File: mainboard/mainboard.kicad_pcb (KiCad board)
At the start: 2 copper layers, 53 x 53 mm, 95 parts, among them J1 USB_B_Micro, J2 Conn_01x19_MountingPin, J3 Conn_01x19_MountingPin, Q1 DMG2301L, Q2 MMBT3904, Q3 MMBT3904, SW1 SW_Push, SW2 SW_Push, U1 ESP32-WROOM-32, U2 tps63070, U3 tps63070, U4 tps63070, U5 CP2102N-A01-GQFN24, U6 BME680, U7 BH1750FVI, U8 LIS3MDL, U9 ADXL343

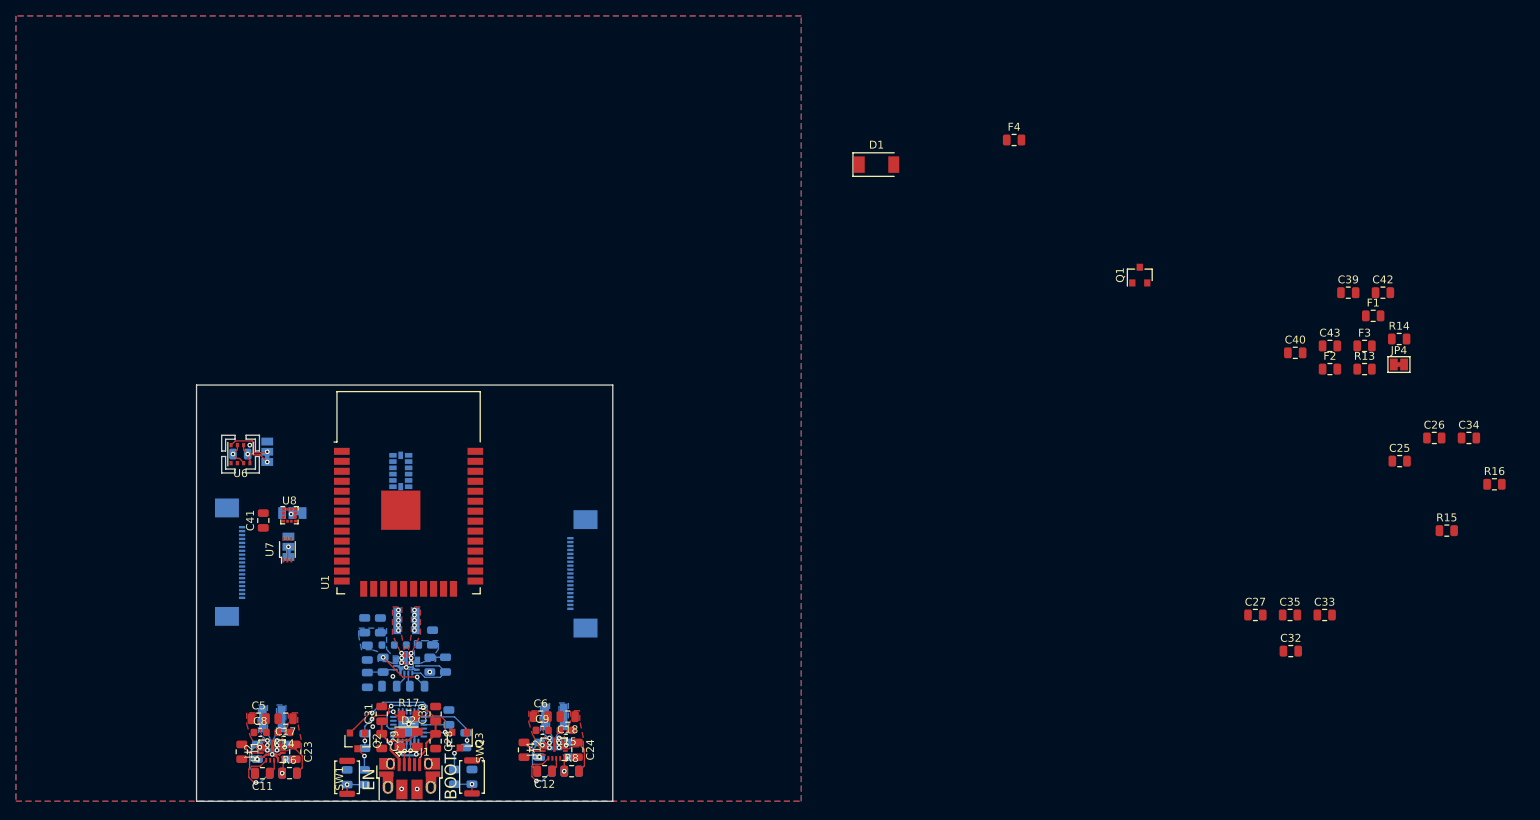
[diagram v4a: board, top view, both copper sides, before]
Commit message: Move components to sane-ish positions
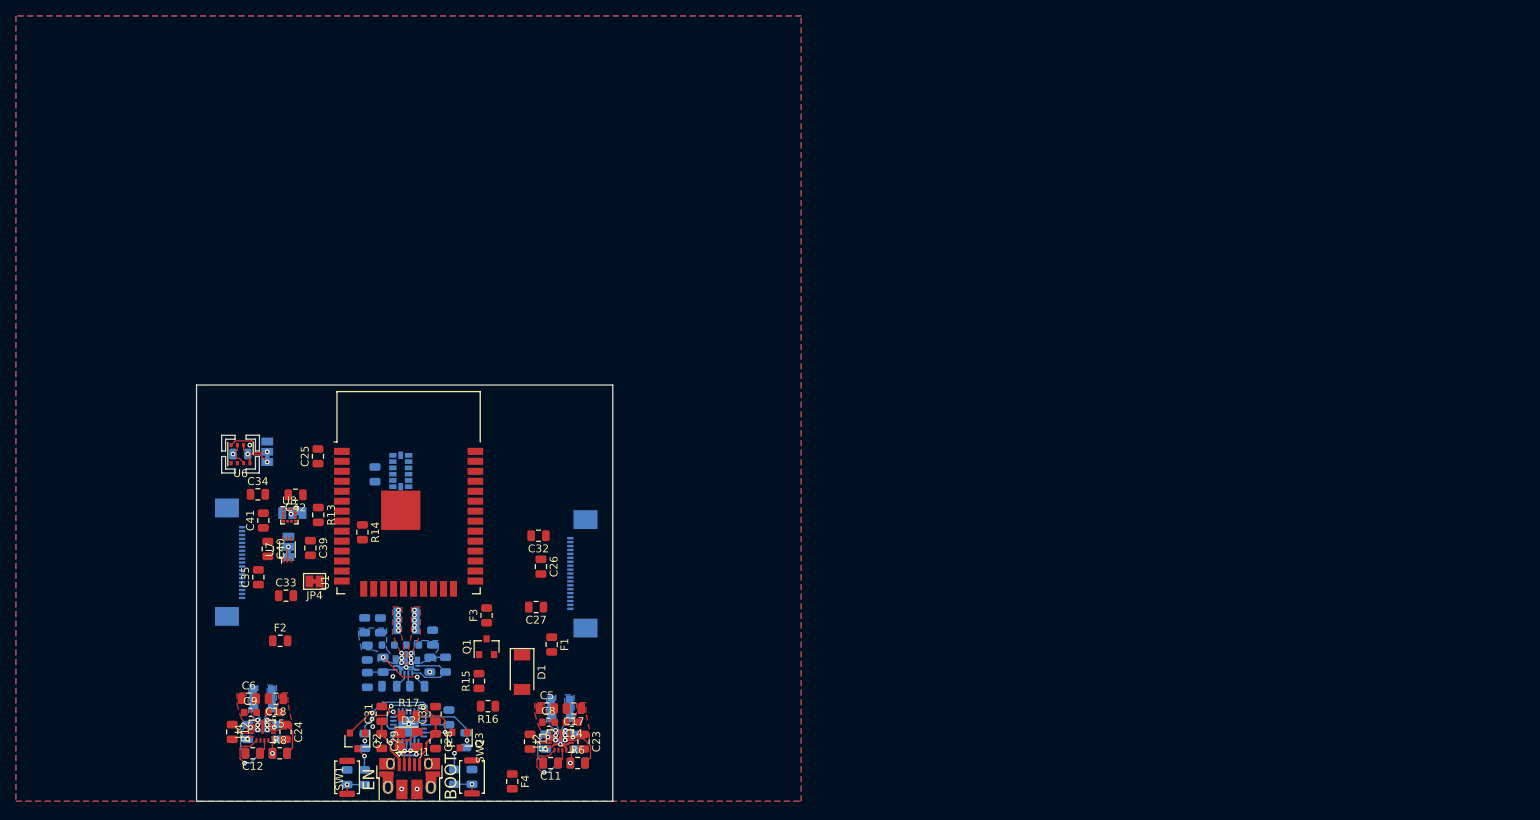
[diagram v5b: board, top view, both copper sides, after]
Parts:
- C43: moved to B.Cu
- moved C34 154.4 mm to (60.8, 90.9)
- moved C42 140.8 mm to (65.6, 91.0), turned to 180 degrees
- moved JP4 140.8 mm to (68.0, 102.0), turned to 180 degrees
- moved F2 138.1 mm to (63.6, 109.6)
- moved C25 137.7 mm to (68.5, 86.1), turned to 90 degrees
- moved C39 136.1 mm to (67.5, 97.8), turned to 270 degrees
- moved R13 134.5 mm to (68.5, 93.5), turned to 270 degrees
- moved R14 134.3 mm to (74.1, 95.8), turned to 270 degrees
- moved C40 133.2 mm to (62.1, 97.9), turned to 270 degrees
- moved C33 132.3 mm to (64.4, 103.8)
- moved C35 131.4 mm to (60.9, 101.5), turned to 90 degrees
- moved R16 131.2 mm to (90.1, 117.9), turned to 180 degrees
- moved R15 124.7 mm to (89.0, 114.7), turned to 90 degrees
- moved C43 122.7 mm to (75.7, 88.4), turned to 90 degrees
- moved F3 116.9 mm to (89.9, 106.3), turned to 90 degrees
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
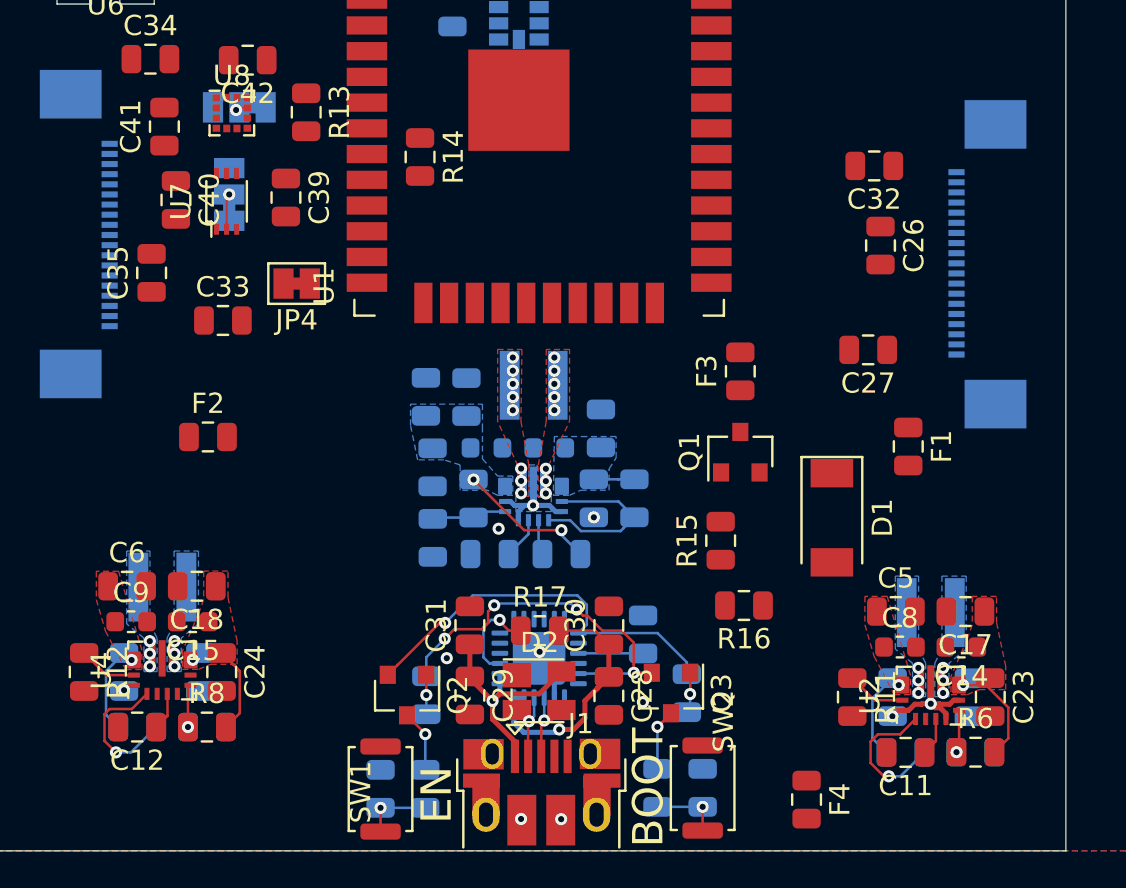
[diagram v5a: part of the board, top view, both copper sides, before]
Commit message: Separate switchmode regulator power and digital ground
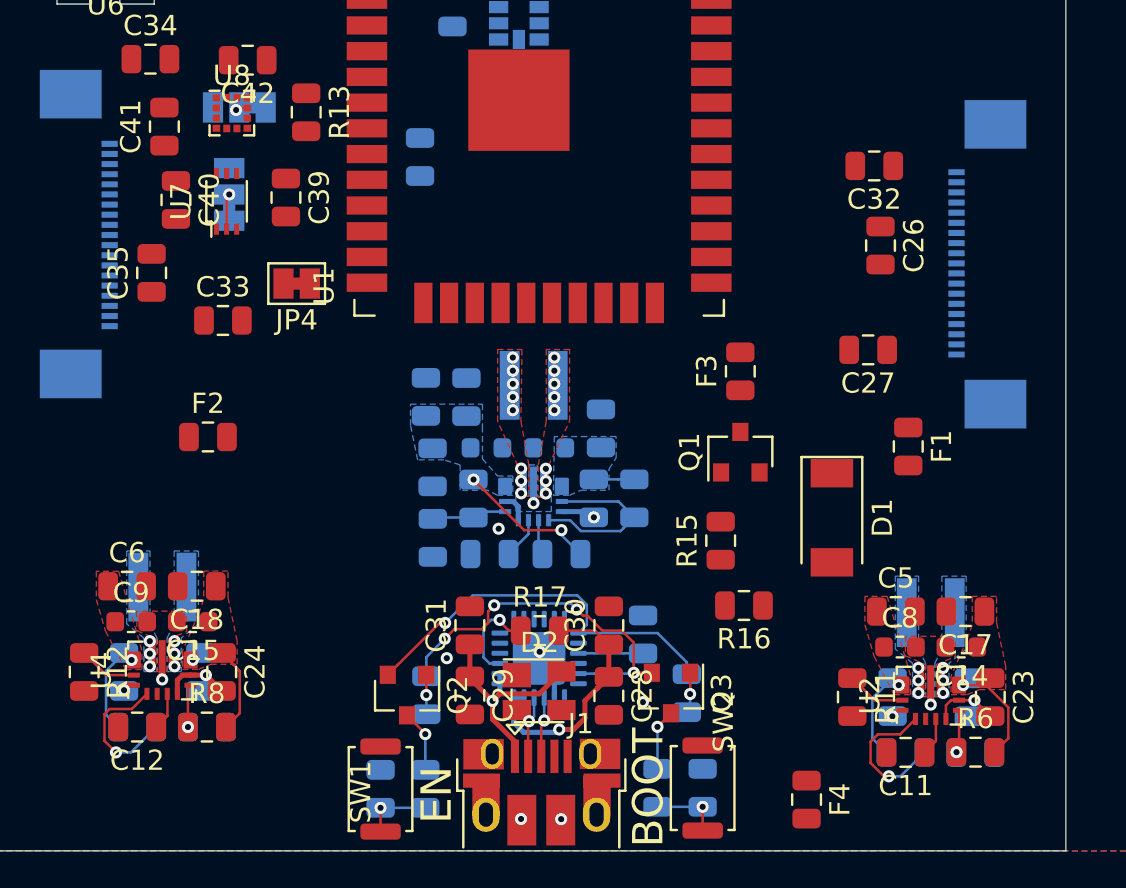
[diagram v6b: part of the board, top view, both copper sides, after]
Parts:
- R14: moved to B.Cu
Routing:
- net GND: track 16.9 -> 21.7 mm, vias 13 -> 16

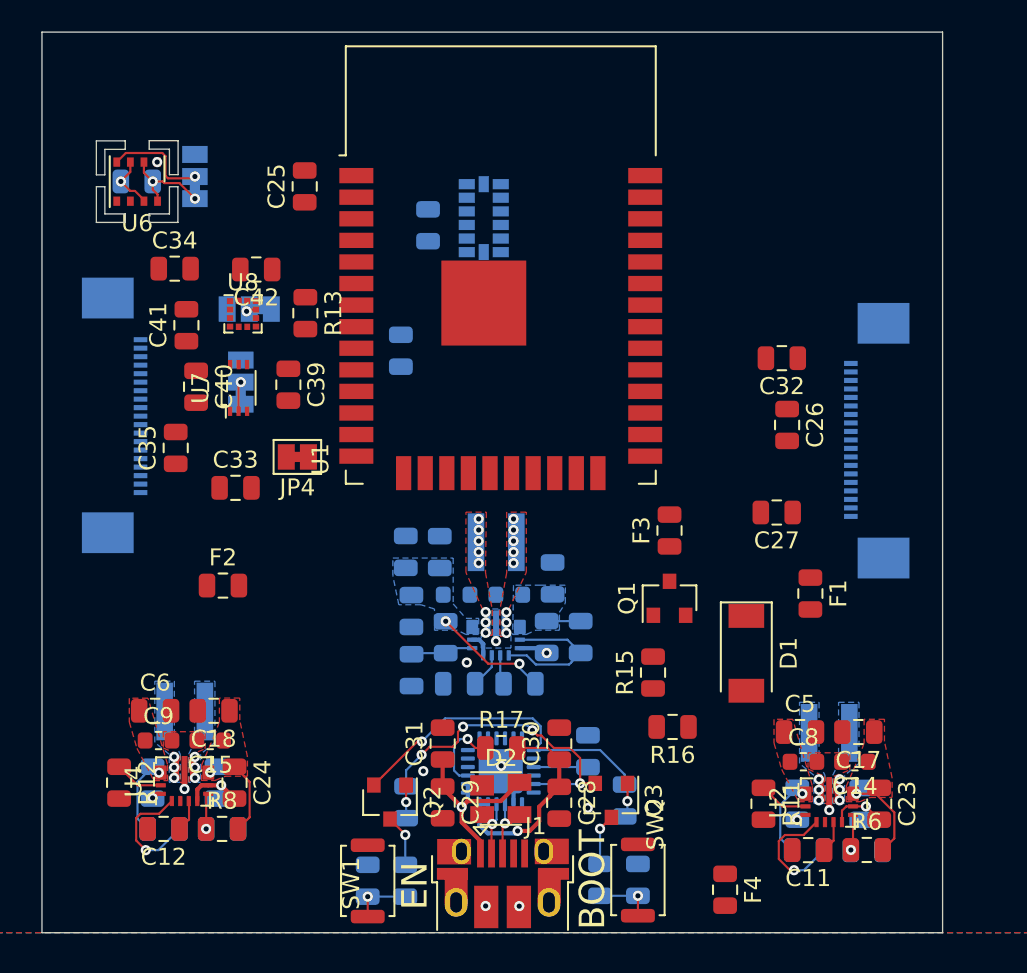
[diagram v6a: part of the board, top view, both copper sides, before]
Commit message: Add right-angle XT30 power connector
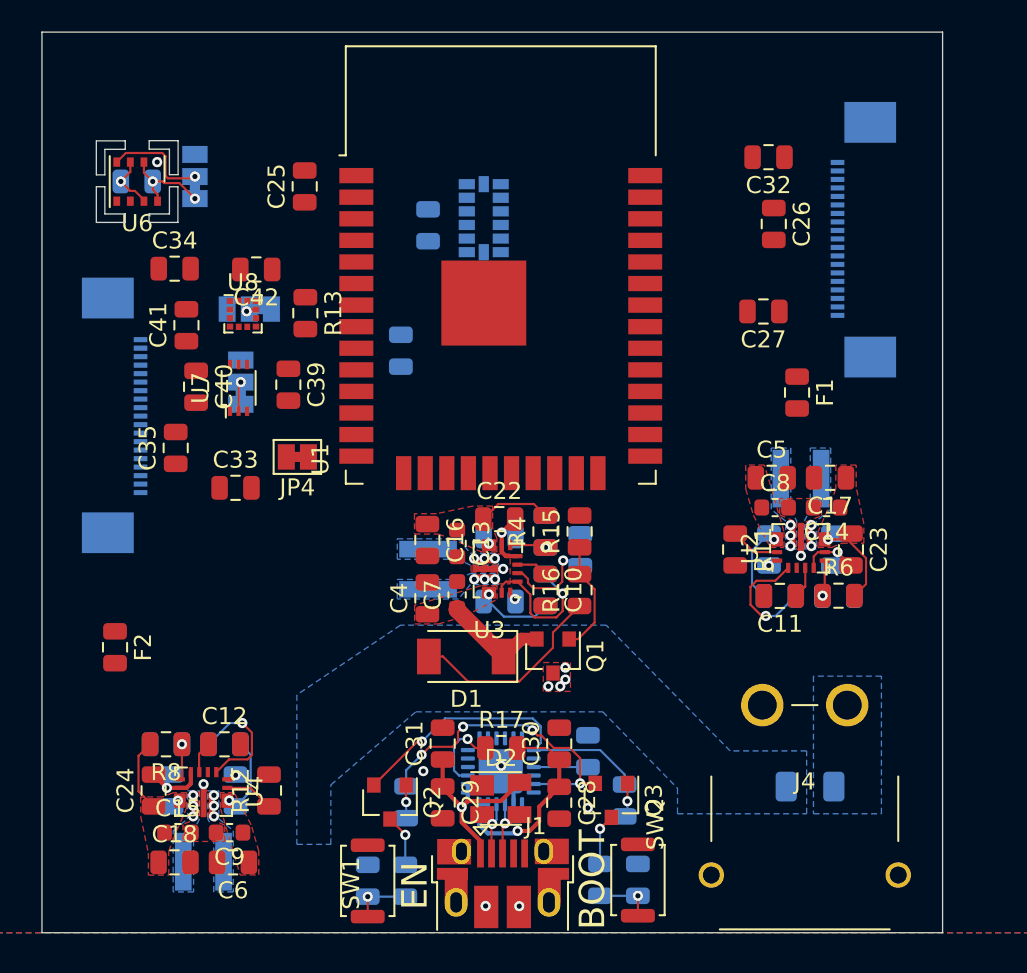
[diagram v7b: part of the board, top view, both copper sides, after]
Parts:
- removed F3: Fuse, Fuse:Fuse_0805_2012Metric
- added J4: Conn_01x02_Male, mainboard:XT30PW, F.Cu at (97.9, 121.6)
- C10, C13, C16, C22, C4, C7, R4, U3: moved to F.Cu
- F4: footprint Fuse:Fuse_0805_2012Metric -> Fuse:Fuse_1206_3216Metric; moved to B.Cu
- moved D1 16.5 mm to (78.0, 113.7), turned to 180 degrees
- moved C11 15.1 mm to (96.4, 110.2)
- moved C14 15.1 mm to (99.2, 105.0)
- moved C17 15.1 mm to (99.4, 103.2)
- moved C2 15.1 mm to (95.8, 107.4)
- moved C20 15.1 mm to (99.5, 107.5)
- moved C23 15.1 mm to (100.6, 107.4)
- moved C5 15.1 mm to (95.9, 103.2)
- moved C8 15.1 mm to (96.1, 105.0)
- moved R11 15.1 mm to (93.8, 107.4)
- moved R2 15.1 mm to (96.4, 110.2)
- moved R7 15.1 mm to (99.9, 110.2)
- moved U2 15.1 mm to (97.7, 107.4)
- moved L2 15.1 mm to (97.7, 103.3)
- moved R6 15.1 mm to (99.9, 110.2)
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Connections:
- Q1 pad 3: Net-(F3-Pad1) -> VDC
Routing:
- net VUSB: track 12.1 -> 24.0 mm
- net VBUS: track 2.00 -> 10.7 mm, vias 0 -> 1
- net Net-(Q1-Pad1): track 0.00 -> 6.70 mm
- net /PG_3V3: track 1.75 -> 5.72 mm, vias 0 -> 1
- net +3V3: track 10.5 -> 7.58 mm, vias 4 -> 3
- net Net-(R4-Pad1): track 4.03 -> 2.13 mm, vias 0 -> 1
- net Net-(R1-Pad1): track 8.64 -> 8.40 mm, vias 0 -> 1
- net VDC: vias 2 -> 6
- net Net-(L1-Pad2): vias 8 -> 3
- net Net-(L1-Pad1): vias 8 -> 3
- added copper zone on F.Cu, net +3V3
- added copper zone on B.Cu, net Net-(F4-Pad2)
- added copper zone on B.Cu, net Net-(L1-Pad1)
- added copper zone on B.Cu, net Net-(L1-Pad2)
- added copper zone on F.Cu, net VBUS
- added copper zone on B.Cu, net VDC
- removed copper zone on B.Cu, net +3V3
- removed copper zone on F.Cu, net Net-(L1-Pad1)
- removed copper zone on F.Cu, net Net-(L1-Pad2)
- removed copper zone on B.Cu, net VBUS

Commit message: More WIP
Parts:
- removed JP1, JP2, JP3: Jumper_3_Bridged12, Jumper:SolderJumper-3_P1.3mm_Bridged12_Pad1.0x1.5mm
- added C44: 1 uC, Capacitor_SMD:C_0805_2012Metric, F.Cu at (70.2, 110.4)
- added D3: LED, LED_SMD:LED_0805_2012Metric, F.Cu at (99.8, 113.1)
- added D4: LED, LED_SMD:LED_0805_2012Metric, F.Cu at (99.8, 110.9)
- added D5: LED, LED_SMD:LED_0805_2012Metric, F.Cu at (99.8, 108.7)
- added D6: LED, LED_SMD:LED_0805_2012Metric, F.Cu at (99.8, 106.5)
- added D7: LED, LED_SMD:LED_0805_2012Metric, F.Cu at (156.2, 89.8)
- added D8: LED, LED_SMD:LED_0805_2012Metric, F.Cu at (62.8, 89.2)
- added D9: LED, LED_SMD:LED_0805_2012Metric, F.Cu at (151.7, 95.9)
- added R23: 1 kR, Resistor_SMD:R_0805_2012Metric, F.Cu at (156.1, 92.8)
- added R24: 330 R, Resistor_SMD:R_0805_2012Metric, F.Cu at (160.6, 89.7)
- added R25: 1 kR, Resistor_SMD:R_0805_2012Metric, F.Cu at (165.0, 86.7)
- added R26: 220 R, Resistor_SMD:R_0805_2012Metric, F.Cu at (156.1, 95.7)
- added R27: 470 R, Resistor_SMD:R_0805_2012Metric, F.Cu at (160.5, 92.8)
- added R28: 470 R, Resistor_SMD:R_0805_2012Metric, F.Cu at (63.7, 85.7)
- added R29: 220 R, Resistor_SMD:R_0805_2012Metric, F.Cu at (160.5, 95.7)
- C33, C34, C35, JP4, R13: moved to B.Cu
- moved C38 30.4 mm to (67.0, 115.0)
- moved U6 30.3 mm to (67.0, 114.9), turned to 270 degrees
- moved C40 22.3 mm to (72.4, 117.7), turned to 180 degrees
- moved C42 19.5 mm to (66.8, 110.4)
- moved U7 19.1 mm to (72.4, 115.3), turned to 180 degrees
- moved C39 16.1 mm to (72.6, 113.0), turned to 0 degrees
- moved U8 14.9 mm to (68.5, 108.0)
- moved C41 14.1 mm to (66.2, 107.6)
- moved C17 11.7 mm to (88.6, 107.6), turned to 270 degrees
- moved L2 10.9 mm to (88.6, 109.3), turned to 90 degrees
- moved C5 10.7 mm to (88.6, 111.1), turned to 90 degrees
- moved C14 9.29 mm to (90.3, 107.8), turned to 270 degrees
- moved C8 8.27 mm to (90.3, 110.9), turned to 90 degrees
- moved JP4 7.90 mm to (68.2, 94.1)
- moved C23 7.87 mm to (92.8, 106.4), turned to 0 degrees
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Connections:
- U1 pad 26: Net-(U1-Pad26) -> /IO4
- U6 pad 5: Net-(JP2-Pad2) -> +3V3
- U7 pad 2: Net-(JP1-Pad2) -> GND
- U8 pad 9: Net-(JP3-Pad2) -> GND
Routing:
- net +3V3: track 7.58 -> 60.3 mm, vias 3 -> 8
- net /PG_VCC1: track 0.00 -> 39.7 mm, vias 0 -> 4
- net /EN: track 3.07 -> 40.6 mm
- net /RXD: track 0.00 -> 34.8 mm, vias 0 -> 3
- net /TXD: track 0.00 -> 32.2 mm, vias 0 -> 3
- net /SCL: track 0.00 -> 28.6 mm, vias 0 -> 2
- net /VCC1_EN: track 2.90 -> 28.7 mm
- net /SDA: track 0.00 -> 25.3 mm, vias 0 -> 2
- net /IO0: track 3.02 -> 25.8 mm
- net /PG_3V3: track 5.72 -> 24.6 mm, vias 1 -> 2
- net VUSB: track 24.0 -> 30.8 mm
- net Net-(JP2-Pad2): track 6.41 -> 0.00 mm, vias 1 -> 0
- net Net-(C15-Pad1): track 4.31 -> 0.00 mm
- net Net-(D8-Pad1): track 0.00 -> 2.57 mm
- net Net-(R3-Pad1): track 7.14 -> 4.64 mm
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- added copper zone on B.Cu, net VCC_EAR1
- added copper zone on F.Cu, net VCC_EAR1
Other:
- board size 53 x 53 mm -> 44.3 x 46.2 mm
- board text added: "3V3"
- board text added: "BUS"
- board text added: "EAR1"
- board text added: "USB"
- board text added: "VDC"
